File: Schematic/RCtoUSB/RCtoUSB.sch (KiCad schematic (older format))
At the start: 18 parts, among them J1 SAT, J2 ICSP, J3 USB_B_Mini, Q1 2N7002P_215, U1 AP2210N-3.3TRG1, U2 PIC18f27J53

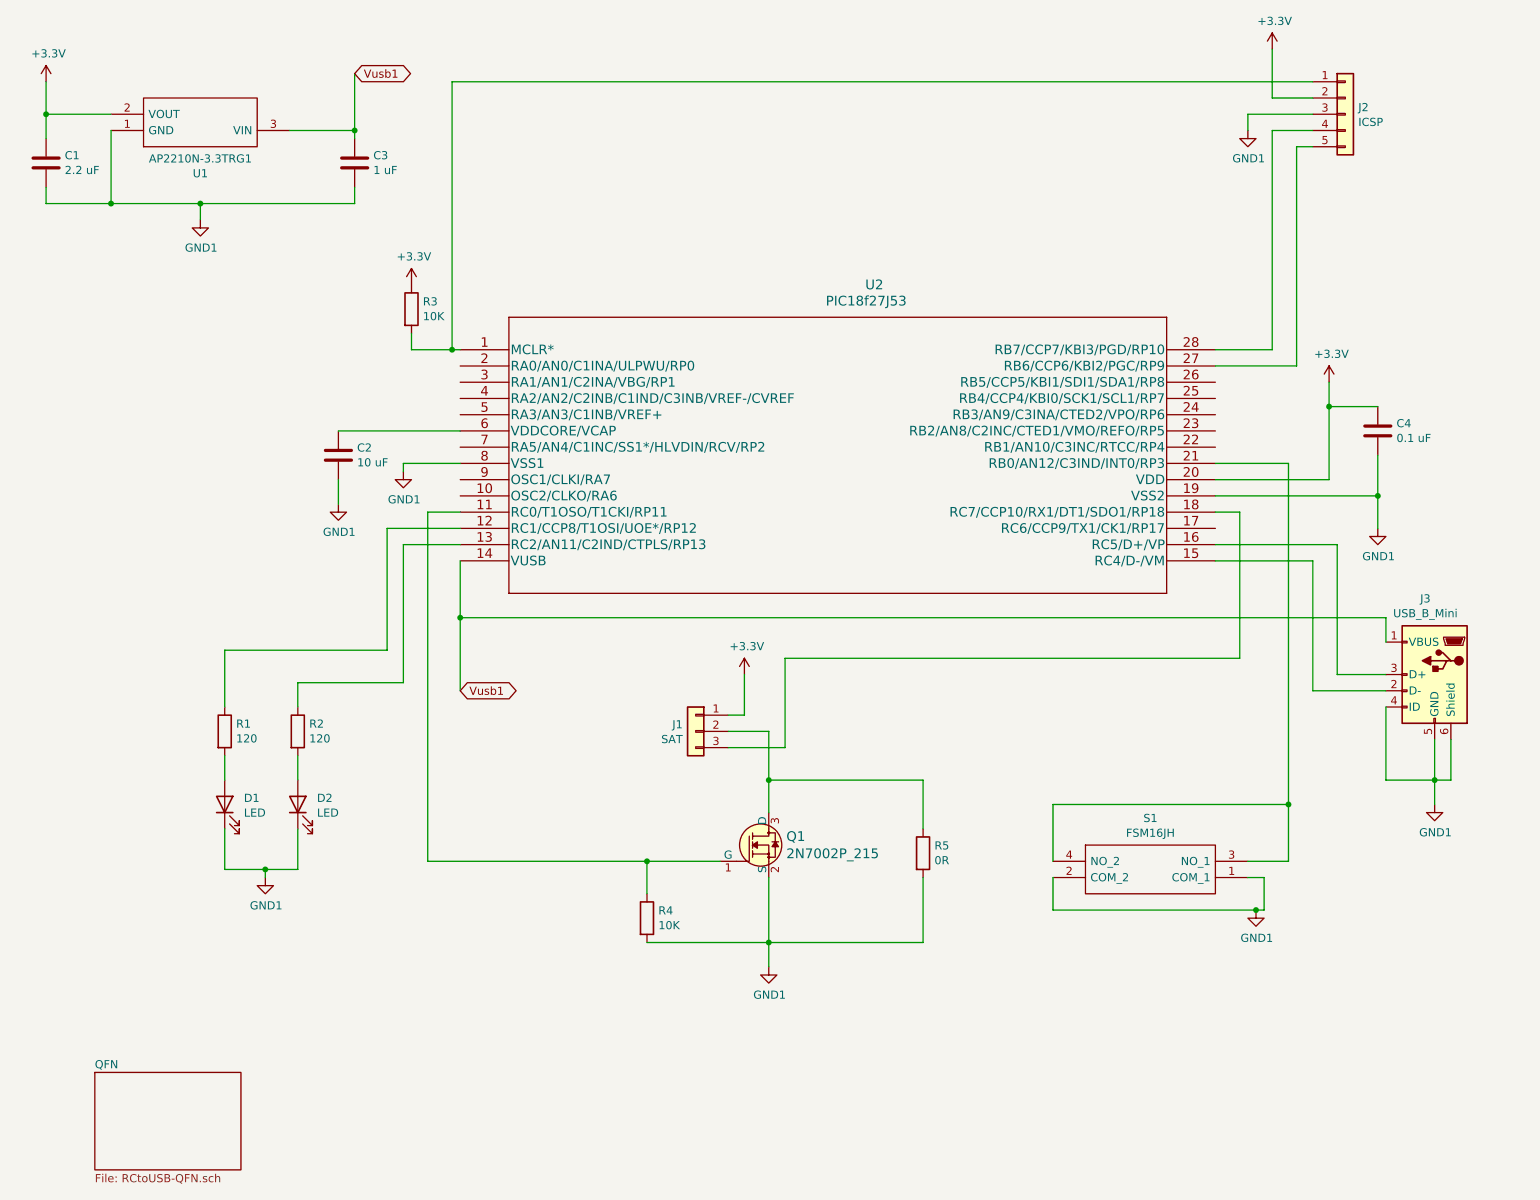
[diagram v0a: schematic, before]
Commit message: Added some breakout connectors to SOIC version
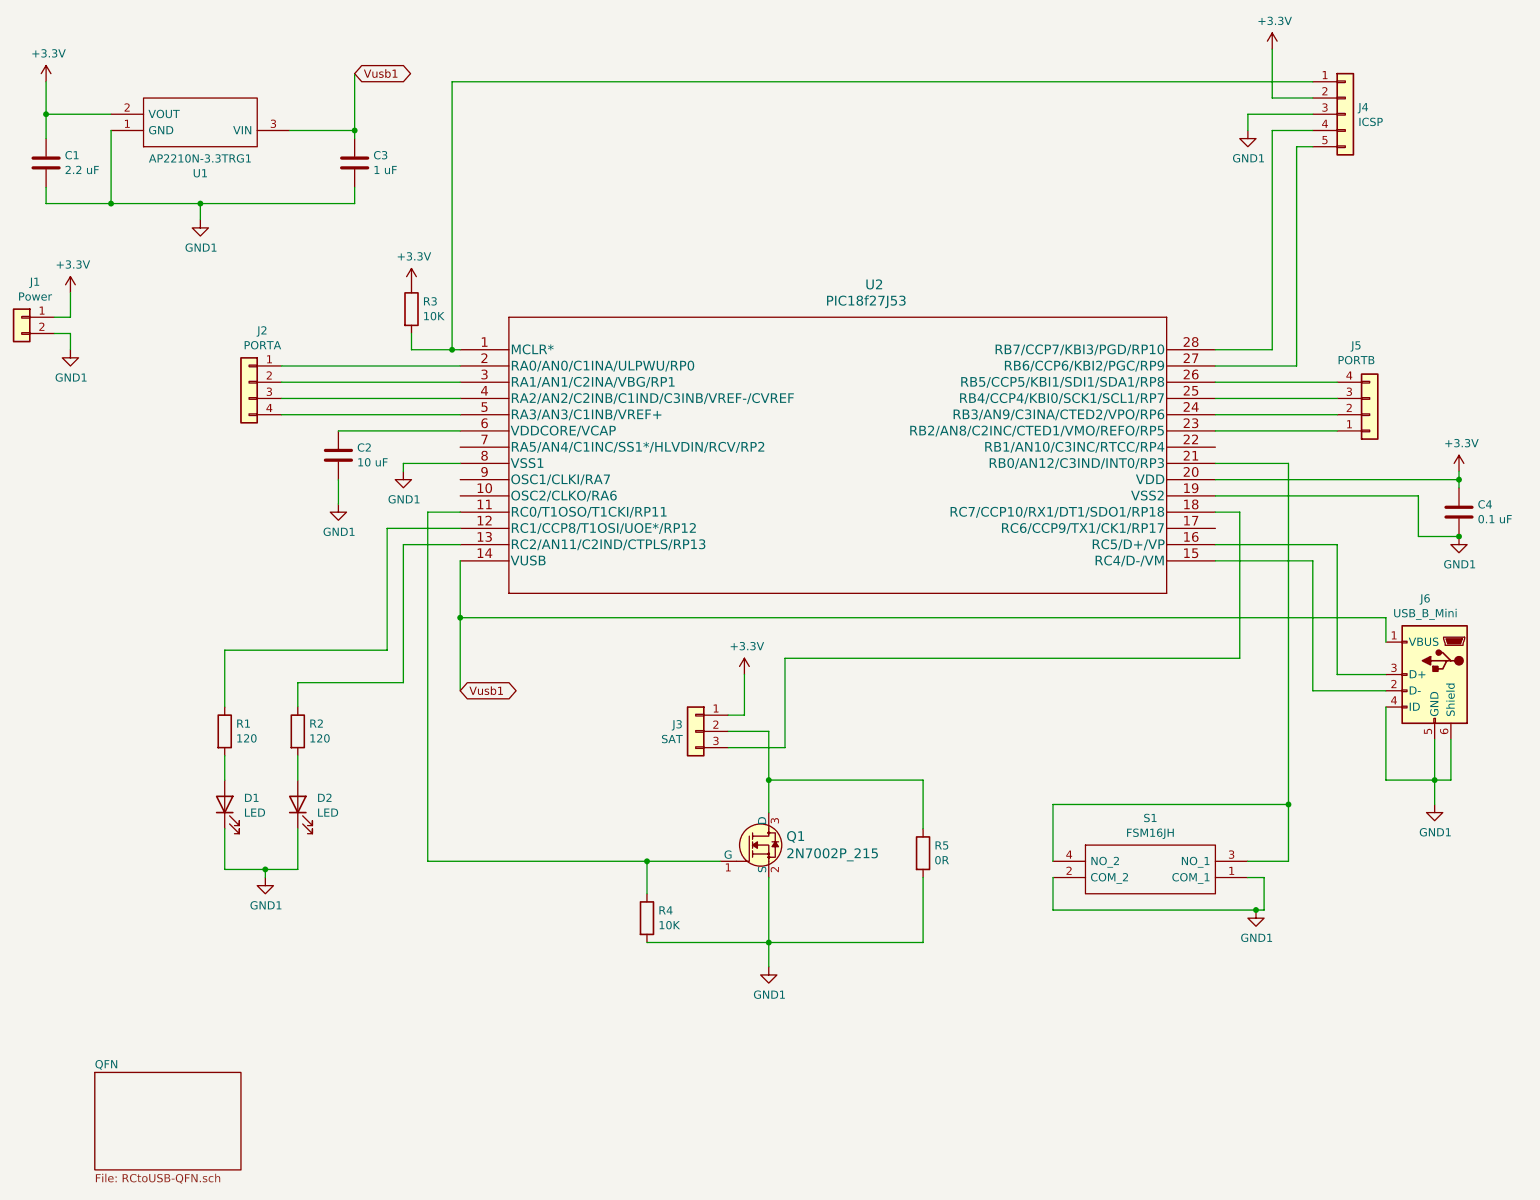
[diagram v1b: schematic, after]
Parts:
- added J1: Power, Connector_PinSocket_2.54mm:PinSocket_1x02_P2.54mm_Vertical_SMD_Pin1Right, symbol Connector_Generic:Conn_01x02
- added J2: PORTA, Connector_PinSocket_2.54mm:PinSocket_1x04_P2.54mm_Vertical_SMD_Pin1Right, symbol Connector_Generic:Conn_01x04
- added J5: PORTB, Connector_PinSocket_2.54mm:PinSocket_1x04_P2.54mm_Vertical_SMD_Pin1Right, symbol Connector_Generic:Conn_01x04
- renumbered J1 to J3, J2 to J4, J3 to J6
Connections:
- net +3V3: now also J1.1 (Pin_1)
- net GND1: now also J1.2 (Pin_2)
- net at U2.2 (RA0/AN0/C1INA/ULPWU/RP0): now also J2.1 (Pin_1)
- net at U2.23 (RB2/AN8/C2INC/CTED1/VMO/REFO/RP5): now also J5.1 (Pin_1)
- net at U2.24 (RB3/AN9/C3INA/CTED2/VPO/RP6): now also J5.2 (Pin_2)
- net at U2.25 (RB4/CCP4/KBI0/SCK1/SCL1/RP7): now also J5.3 (Pin_3)
- net at U2.26 (RB5/CCP5/KBI1/SDI1/SDA1/RP8): now also J5.4 (Pin_4)
- net at U2.3 (RA1/AN1/C2INA/VBG/RP1): now also J2.2 (Pin_2)
- net at U2.4 (RA2/AN2/C2INB/C1IND/C3INB/VREF-/CVREF): now also J2.3 (Pin_3)
- net at U2.5 (RA3/AN3/C1INB/VREF+): now also J2.4 (Pin_4)
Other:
- moved on the sheet: C4
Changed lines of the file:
@@
 $EndComp
 $Comp
-L Connector_Generic:Conn_01x05 J2
+L Connector_Generic:Conn_01x05 J4
 U 1 1 60FB842F
 P 8900 1150
-F 0 "J2" H 8980 1192 50  0000 L CNN
+F 0 "J4" H 8980 1192 50  0000 L CNN
 F 1 "ICSP" H 8980 1101 50  0000 L CNN
 F 2 "Connector_PinHeader_2.54mm:PinHeader_1x05_P2.54mm_Vertical" H 8900 1150 50  0001 C CNN
@@
 $EndComp
 $Comp
-L Connector_Generic:Conn_01x03 J1
+L Connector_Generic:Conn_01x03 J3
 U 1 1 60FB92FD
 P 4900 4950
-F 0 "J1" H 4980 4992 50  0000 L CNN
+F 0 "J3" H 4980 4992 50  0000 L CNN
 F 1 "SAT" H 4980 4901 50  0000 L CNN
 F 2 "JST-withZH:JST_ZH_B3B-ZR_1x03_P1.50mm_Vertical" H 4900 4950 50  0001 C CNN
@@
 $EndComp
 $Comp
-L power:GND1 #PWR05
+L power:GND1 #PWR07
 U 1 1 60FB1F3D
 P 3100 3350
-F 0 "#PWR05" H 3100 3100 50  0001 C CNN
+F 0 "#PWR07" H 3100 3100 50  0001 C CNN
 F 1 "GND1" H 3105 3177 50  0000 C CNN
 F 2 "" H 3100 3350 50  0001 C CNN
@@
 	9450 5250 9450 5400
 $Comp
-L power:GND1 #PWR02
+L power:GND1 #PWR04
 U 1 1 60FB58ED
 P 1850 1800
-F 0 "#PWR02" H 1850 1550 50  0001 C CNN
+F 0 "#PWR04" H 1850 1550 50  0001 C CNN
 F 1 "GND1" H 1855 1627 50  0000 C CNN
 F 2 "" H 1850 1800 50  0001 C CNN
@@
 $EndComp
 $Comp
-L power:+3.3V #PWR012
+L power:+3.3V #PWR015
 U 1 1 60FB8B23
-P 8800 2800
-F 0 "#PWR012" H 8800 2650 50  0001 C CNN
-F 1 "+3.3V" H 8815 2973 50  0000 C CNN
-F 2 "" H 8800 2800 50  0001 C CNN
-F 3 "" H 8800 2800 50  0001 C CNN
-	1    8800 2800
-	1    0    0    -1
-$EndComp
-$Comp
-L power:GND1 #PWR013
+P 9600 3350
+F 0 "#PWR015" H 9600 3200 50  0001 C CNN
+F 1 "+3.3V" H 9615 3523 50  0000 C CNN
+F 2 "" H 9600 3350 50  0001 C CNN
+F 3 "" H 9600 3350 50  0001 C CNN
+	1    9600 3350
+	1    0    0    -1
+$EndComp
+$Comp
+L power:GND1 #PWR016
 U 1 1 60FBA1D6
-P 9100 3700
-F 0 "#PWR013" H 9100 3450 50  0001 C CNN
-F 1 "GND1" H 9105 3527 50  0000 C CNN
-F 2 "" H 9100 3700 50  0001 C CNN
-F 3 "" H 9100 3700 50  0001 C CNN
-	1    9100 3700
-	1    0    0    -1
-$EndComp
-$Comp
-L power:+3.3V #PWR06
+P 9600 3750
+F 0 "#PWR016" H 9600 3500 50  0001 C CNN
+F 1 "GND1" H 9605 3577 50  0000 C CNN
+F 2 "" H 9600 3750 50  0001 C CNN
+F 3 "" H 9600 3750 50  0001 C CNN
+	1    9600 3750
+	1    0    0    -1
+$EndComp
+$Comp
+L power:+3.3V #PWR08
 U 1 1 60FBA91E
 P 3150 2200
-F 0 "#PWR06" H 3150 2050 50  0001 C CNN
+F 0 "#PWR08" H 3150 2050 50  0001 C CNN
 F 1 "+3.3V" H 3165 2373 50  0000 C CNN
 F 2 "" H 3150 2200 50  0001 C CNN
@@
 $EndComp
 $Comp
-L power:GND1 #PWR03
+L power:GND1 #PWR05
 U 1 1 60FBB205
 P 2250 5850
-F 0 "#PWR03" H 2250 5600 50  0001 C CNN
+F 0 "#PWR05" H 2250 5600 50  0001 C CNN
 F 1 "GND1" H 2255 5677 50  0000 C CNN
 F 2 "" H 2250 5850 50  0001 C CNN
@@
 $EndComp
 $Comp
-L power:GND1 #PWR09
+L power:GND1 #PWR011
 U 1 1 60FBF2C7
 P 8300 1250
-F 0 "#PWR09" H 8300 1000 50  0001 C CNN
+F 0 "#PWR011" H 8300 1000 50  0001 C CNN
 F 1 "GND1" H 8305 1077 50  0000 C CNN
 F 2 "" H 8300 1250 50  0001 C CNN
@@
 	8300 1150 8300 1250
 $Comp
-L power:+3.3V #PWR011
+L power:+3.3V #PWR013
 U 1 1 60FC04DF
 P 8450 750
-F 0 "#PWR011" H 8450 600 50  0001 C CNN
+F 0 "#PWR013" H 8450 600 50  0001 C CNN
 F 1 "+3.3V" H 8465 923 50  0000 C CNN
 F 2 "" H 8450 750 50  0001 C CNN
@@
 $EndComp
 $Comp
-L power:GND1 #PWR010
+L power:GND1 #PWR012
 U 1 1 60FC2FDD
 P 8350 6050
-F 0 "#PWR010" H 8350 5800 50  0001 C CNN
+F 0 "#PWR012" H 8350 5800 50  0001 C CNN
 F 1 "GND1" H 8355 5877 50  0000 C CNN
 F 2 "" H 8350 6050 50  0001 C CNN
@@
 $EndComp
 $Comp
-L Connector:USB_B_Mini J3
+L Connector:USB_B_Mini J6
 U 1 1 60FB39F8
 P 9450 4600
-F 0 "J3" H 9507 5067 50  0000 C CNN
+F 0 "J6" H 9507 5067 50  0000 C CNN
 F 1 "USB_B_Mini" H 9507 4976 50  0000 C CNN
 F 2 "Connector_USB:USB_Mini-B_Wuerth_65100516121_Horizontal" H 9600 4550 50  0001 C CNN
@@
 	1    9450 4600
 	-1   0    0    -1
-$EndComp
-$Comp
-L Device:C C4
-U 1 1 60FB22D7
-P 9100 3100
-F 0 "C4" H 9215 3146 50  0000 L CNN
-F 1 "0.1 uF" H 9215 3055 50  0000 L CNN
-F 2 "Capacitor_SMD:C_0805_2012Metric" H 9138 2950 50  0001 C CNN
-F 3 "~" H 9100 3100 50  0001 C CNN
-	1    9100 3100
-	1    0    0    -1
 $EndComp
 $Comp
@@
 	1300 1700 1850 1700
 Wire Wire Line
-	8100 3400 8800 3400
-Wire Wire Line
-	8800 3400 8800 2950
-Wire Wire Line
-	9100 2950 8800 2950
-Connection ~ 8800 2950
-Wire Wire Line
-	8800 2950 8800 2800
-Wire Wire Line
 	3450 3300 3100 3300
 Wire Wire Line
 	3100 3300 3100 3350
 $Comp
-L power:GND1 #PWR04
+L power:GND1 #PWR06
 U 1 1 60FD4618
 P 2700 3550
-F 0 "#PWR04" H 2700 3300 50  0001 C CNN
+F 0 "#PWR06" H 2700 3300 50  0001 C CNN
 F 1 "GND1" H 2705 3377 50  0000 C CNN
 F 2 "" H 2700 3550 50  0001 C CNN
@@
 Connection ~ 2250 5800
 $Comp
-L power:+3.3V #PWR07
+L power:+3.3V #PWR09
 U 1 1 60FEEACC
 P 5200 4600
-F 0 "#PWR07" H 5200 4450 50  0001 C CNN
+F 0 "#PWR09" H 5200 4450 50  0001 C CNN
 F 1 "+3.3V" H 5215 4773 50  0000 C CNN
 F 2 "" H 5200 4600 50  0001 C CNN
@@
 	5350 4950 5350 5250
 $Comp
-L power:GND1 #PWR08
+L power:GND1 #PWR010
 U 1 1 60FF497A
 P 5350 6400
-F 0 "#PWR08" H 5350 6150 50  0001 C CNN
+F 0 "#PWR010" H 5350 6150 50  0001 C CNN
 F 1 "GND1" H 5355 6227 50  0000 C CNN
 F 2 "" H 5350 6400 50  0001 C CNN
@@
 Wire Wire Line
 	6300 6250 5350 6250
-Wire Wire Line
-	9100 3250 9100 3500
-Wire Wire Line
-	8100 3500 9100 3500
-Connection ~ 9100 3500
-Wire Wire Line
-	9100 3500 9100 3700
 Wire Wire Line
 	8550 3300 8550 5400
@@
 F1 "RCtoUSB-QFN.sch" 50
 $EndSheet
+$Comp
+L Connector_Generic:Conn_01x04 J2
+U 1 1 60FDCDFA
+P 2150 2800
+F 0 "J2" H 2068 3117 50  0000 C CNN
+F 1 "PORTA" H 2068 3026 50  0000 C CNN
+F 2 "Connector_PinSocket_2.54mm:PinSocket_1x04_P2.54mm_Vertical_SMD_Pin1Right" H 2150 2800 50  0001 C CNN
+F 3 "~" H 2150 2800 50  0001 C CNN
+	1    2150 2800
+	-1   0    0    -1
+$EndComp
+$Comp
+L Connector_Generic:Conn_01x04 J5
+U 1 1 60FDDD5C
+P 9050 3000
+F 0 "J5" H 8968 2575 50  0000 C CNN
+F 1 "PORTB" H 8968 2666 50  0000 C CNN
+F 2 "Connector_PinSocket_2.54mm:PinSocket_1x04_P2.54mm_Vertical_SMD_Pin1Right" H 9050 3000 50  0001 C CNN
+F 3 "~" H 9050 3000 50  0001 C CNN
+	1    9050 3000
+	1    0    0    1
+$EndComp
+$Comp
+L Connector_Generic:Conn_01x02 J1
+U 1 1 60FDEA17
+P 750 2400
+F 0 "J1" H 668 2617 50  0000 C CNN
+F 1 "Power" H 668 2526 50  0000 C CNN
+F 2 "Connector_PinSocket_2.54mm:PinSocket_1x02_P2.54mm_Vertical_SMD_Pin1Right" H 750 2400 50  0001 C CNN
+F 3 "~" H 750 2400 50  0001 C CNN
+	1    750  2400
+	-1   0    0    -1
+$EndComp
+$Comp
+L Device:C C4
+U 1 1 60FB22D7
+P 9600 3600
+F 0 "C4" H 9715 3646 50  0000 L CNN
+F 1 "0.1 uF" H 9715 3555 50  0000 L CNN
+F 2 "Capacitor_SMD:C_0805_2012Metric" H 9638 3450 50  0001 C CNN
+F 3 "~" H 9600 3600 50  0001 C CNN
+	1    9600 3600
+	1    0    0    -1
+$EndComp
+Wire Wire Line
+	8100 3400 9600 3400
+Wire Wire Line
+	9600 3400 9600 3450
+Wire Wire Line
+	9600 3350 9600 3400
+Connection ~ 9600 3400
+Wire Wire Line
+	8100 3500 9350 3500
+Wire Wire Line
+	9350 3500 9350 3750
+Wire Wire Line
+	9350 3750 9600 3750
+Connection ~ 9600 3750
+Wire Wire Line
+	8100 3100 8850 3100
+Wire Wire Line
+	8100 3000 8850 3000
+Wire Wire Line
+	8100 2900 8850 2900
+Wire Wire Line
+	8100 2800 8850 2800
+Wire Wire Line
+	3450 2700 2350 2700
+Wire Wire Line
+	3450 2800 2350 2800
+Wire Wire Line
+	3450 2900 2350 2900
+Wire Wire Line
+	3450 3000 2350 3000
+$Comp
+L power:GND1 #PWR03
+U 1 1 6101483F
+P 1050 2600
+F 0 "#PWR03" H 1050 2350 50  0001 C CNN
+F 1 "GND1" H 1055 2427 50  0000 C CNN
+F 2 "" H 1050 2600 50  0001 C CNN
+F 3 "" H 1050 2600 50  0001 C CNN
+	1    1050 2600
+	1    0    0    -1
+$EndComp
+$Comp
+L power:+3.3V #PWR02
+U 1 1 61015187
+P 1050 2250
+F 0 "#PWR02" H 1050 2100 50  0001 C CNN
+F 1 "+3.3V" H 1065 2423 50  0000 C CNN
+F 2 "" H 1050 2250 50  0001 C CNN
+F 3 "" H 1050 2250 50  0001 C CNN
+	1    1050 2250
+	1    0    0    -1
+$EndComp
+Wire Wire Line
+	950  2400 1050 2400
+Wire Wire Line
+	1050 2400 1050 2250
+Wire Wire Line
+	950  2500 1050 2500
+Wire Wire Line
+	1050 2500 1050 2600
 $EndSCHEMATC

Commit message: Fixed footprints for breakout connectors
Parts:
- J1: footprint Connector_PinSocket_2.54mm:PinSocket_1x02_P2.54mm_Vertical_SMD_Pin1Right -> Connector_PinSocket_2.54mm:PinSocket_1x02_P2.54mm_Vertical
- J2, J5: footprint Connector_PinSocket_2.54mm:PinSocket_1x04_P2.54mm_Vertical_SMD_Pin1Right -> Connector_PinSocket_2.54mm:PinSocket_1x04_P2.54mm_Vertical
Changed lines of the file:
@@
 F 0 "J2" H 2068 3117 50  0000 C CNN
 F 1 "PORTA" H 2068 3026 50  0000 C CNN
-F 2 "Connector_PinSocket_2.54mm:PinSocket_1x04_P2.54mm_Vertical_SMD_Pin1Right" H 2150 2800 50  0001 C CNN
+F 2 "Connector_PinSocket_2.54mm:PinSocket_1x04_P2.54mm_Vertical" H 2150 2800 50  0001 C CNN
 F 3 "~" H 2150 2800 50  0001 C CNN
 	1    2150 2800
@@
 F 0 "J5" H 8968 2575 50  0000 C CNN
 F 1 "PORTB" H 8968 2666 50  0000 C CNN
-F 2 "Connector_PinSocket_2.54mm:PinSocket_1x04_P2.54mm_Vertical_SMD_Pin1Right" H 9050 3000 50  0001 C CNN
+F 2 "Connector_PinSocket_2.54mm:PinSocket_1x04_P2.54mm_Vertical" H 9050 3000 50  0001 C CNN
 F 3 "~" H 9050 3000 50  0001 C CNN
 	1    9050 3000
@@
 F 0 "J1" H 668 2617 50  0000 C CNN
 F 1 "Power" H 668 2526 50  0000 C CNN
-F 2 "Connector_PinSocket_2.54mm:PinSocket_1x02_P2.54mm_Vertical_SMD_Pin1Right" H 750 2400 50  0001 C CNN
+F 2 "Connector_PinSocket_2.54mm:PinSocket_1x02_P2.54mm_Vertical" H 750 2400 50  0001 C CNN
 F 3 "~" H 750 2400 50  0001 C CNN
 	1    750  2400

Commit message: Finished schematic and pcb
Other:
- note added: "Do not populate R5"
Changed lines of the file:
@@
 	1    0    0    -1
 $EndComp
+Text Notes 5900 5950 0    50   ~ 0
+Do not populate R5
 $EndSCHEMATC

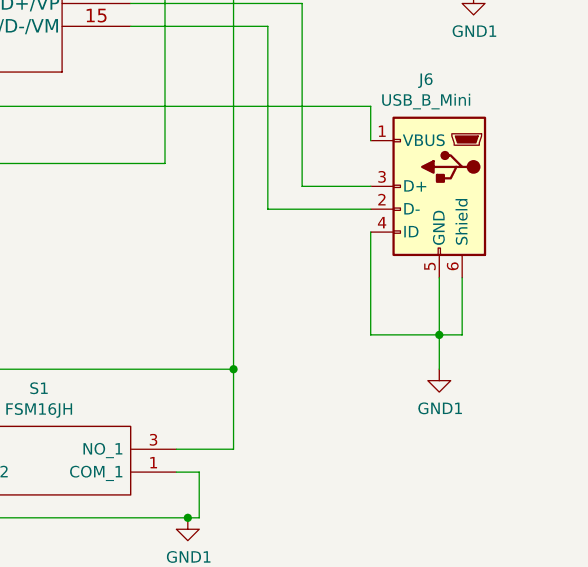
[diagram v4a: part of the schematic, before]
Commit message: Changed ID pin to floating on USB connector
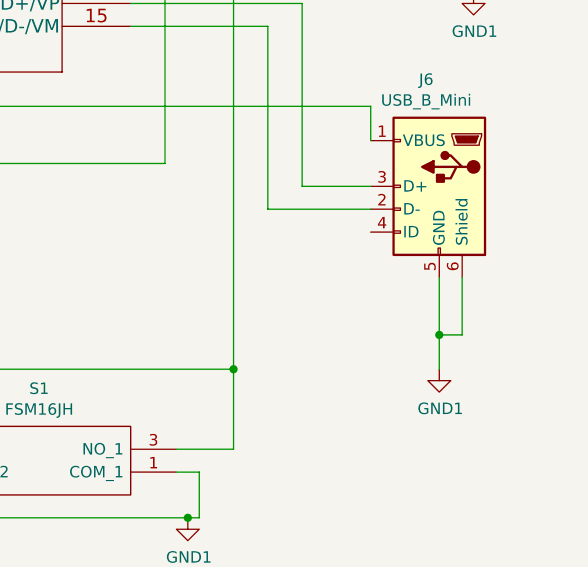
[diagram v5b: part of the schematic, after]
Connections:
- net GND1: no longer J6.4 (ID)
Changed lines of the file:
@@
 	8600 1350 8700 1350
-Wire Wire Line
-	9150 4800 9150 5250
-Wire Wire Line
-	9150 5250 9450 5250
 Wire Wire Line
 	9450 5000 9450 5250
